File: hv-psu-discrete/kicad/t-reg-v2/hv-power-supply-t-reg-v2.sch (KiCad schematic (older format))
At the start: 107 parts, among them J1 AC-HV, J10 HV, J11 GND_HV, J12 LED, J13 GND_LED, J14 +5V, J15 GND_5V, J2 AC-HV, J3 EARTH, J4 AC-LV, J5 AC-LV, J6 LV1, J7 GND_LV1, K1 G6S-2 DC5, Q1 FDP12N60NZ, Q2 MMBT3904-TP, Q3 BC850, Q4 IXTP1R6N50D2, Q5 BC860, Q6 BC850, SW1 SW_Push, U1 LT3092xST, U2 LM7805_TO220, U3 AD8031, U4 LM317_3PinPackage, U6 TLC555CDR

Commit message: layout completed
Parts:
- D1, D2, D7, D8: value BYV98-200 -> BYG22B-E3; footprint kicad-snk:SOD64-10 -> Diode_SMD:D_SMA_Handsoldering
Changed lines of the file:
@@
 Sheet 1 1
 Title "Discrete HV Supply T-Reg based"
-Date "2021-08-21"
-Rev "V1a"
+Date "2021-09-02"
+Rev "V2"
 Comp ""
 Comment1 ""
@@
 P 3450 9150
 F 0 "D1" H 3450 9367 50  0000 C CNN
-F 1 "BYV98-200" H 3450 9276 50  0000 C CNN
-F 2 "kicad-snk:SOD64-10" H 3450 9150 50  0001 C CNN
+F 1 "BYG22B-E3" H 3450 9276 50  0000 C CNN
+F 2 "Diode_SMD:D_SMA_Handsoldering" H 3450 9150 50  0001 C CNN
 F 3 "~" H 3450 9150 50  0001 C CNN
 	1    3450 9150
@@
 P 3450 9750
 F 0 "D2" H 3450 9967 50  0000 C CNN
-F 1 "BYV98-200" H 3450 9876 50  0000 C CNN
-F 2 "kicad-snk:SOD64-10" H 3450 9750 50  0001 C CNN
+F 1 "BYG22B-E3" H 3450 9876 50  0000 C CNN
+F 2 "Diode_SMD:D_SMA_Handsoldering" H 3450 9750 50  0001 C CNN
 F 3 "~" H 3450 9750 50  0001 C CNN
 	1    3450 9750
@@
 P 3950 9150
 F 0 "D7" H 3950 9367 50  0000 C CNN
-F 1 "BYV98-200" H 3950 9276 50  0000 C CNN
-F 2 "kicad-snk:SOD64-10" H 3950 9150 50  0001 C CNN
+F 1 "BYG22B-E3" H 3950 9276 50  0000 C CNN
+F 2 "Diode_SMD:D_SMA_Handsoldering" H 3950 9150 50  0001 C CNN
 F 3 "~" H 3950 9150 50  0001 C CNN
 	1    3950 9150
@@
 P 3950 9750
 F 0 "D8" H 3950 9967 50  0000 C CNN
-F 1 "BYV98-200" H 3950 9876 50  0000 C CNN
-F 2 "kicad-snk:SOD64-10" H 3950 9750 50  0001 C CNN
+F 1 "BYG22B-E3" H 3950 9876 50  0000 C CNN
+F 2 "Diode_SMD:D_SMA_Handsoldering" H 3950 9750 50  0001 C CNN
 F 3 "~" H 3950 9750 50  0001 C CNN
 	1    3950 9750

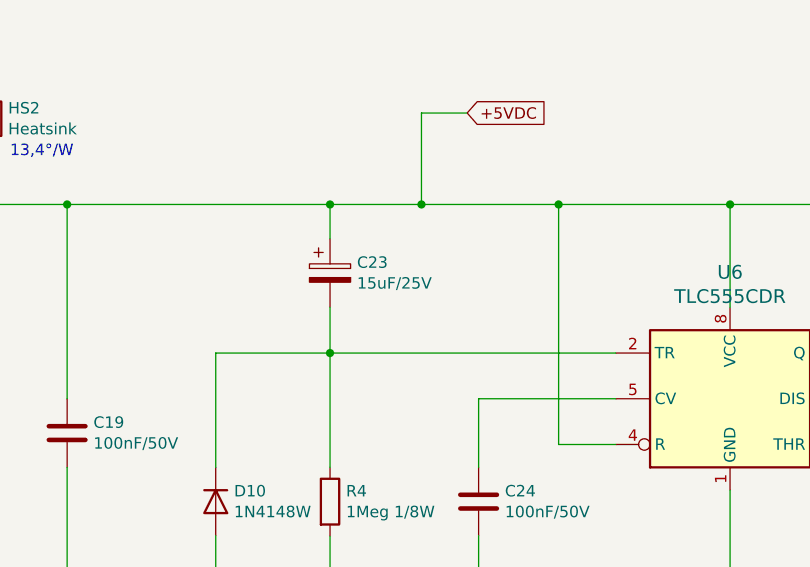
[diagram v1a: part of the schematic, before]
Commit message: replace tantal with smaller one
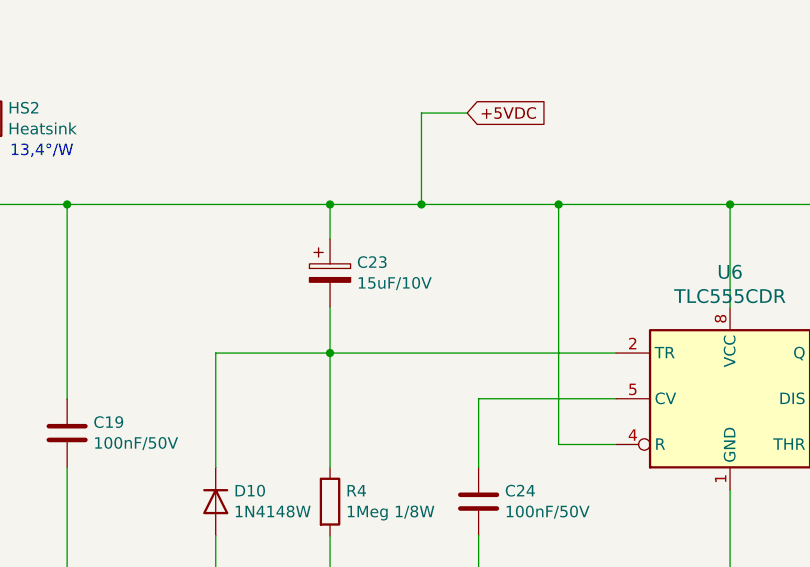
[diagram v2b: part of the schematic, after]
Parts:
- C23: value 15uF/25V -> 15uF/10V; footprint Capacitor_Tantalum_SMD:CP_EIA-7343-31_Kemet-D_Pad2.25x2.55mm_HandSolder -> Capacitor_Tantalum_SMD:CP_EIA-3216-12_Kemet-S_Pad1.58x1.35mm_HandSolder
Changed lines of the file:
@@
 P 7800 8800
 F 0 "C23" H 7918 8846 50  0000 L CNN
-F 1 "15uF/25V" H 7918 8755 50  0000 L CNN
-F 2 "Capacitor_Tantalum_SMD:CP_EIA-7343-31_Kemet-D_Pad2.25x2.55mm_HandSolder" H 7838 8650 50  0001 C CNN
+F 1 "15uF/10V" H 7918 8755 50  0000 L CNN
+F 2 "Capacitor_Tantalum_SMD:CP_EIA-3216-12_Kemet-S_Pad1.58x1.35mm_HandSolder" H 7838 8650 50  0001 C CNN
 F 3 "~" H 7800 8800 50  0001 C CNN
 	1    7800 8800
